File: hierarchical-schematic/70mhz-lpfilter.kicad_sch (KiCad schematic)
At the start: 11 parts, among them J701 In, J702 Out

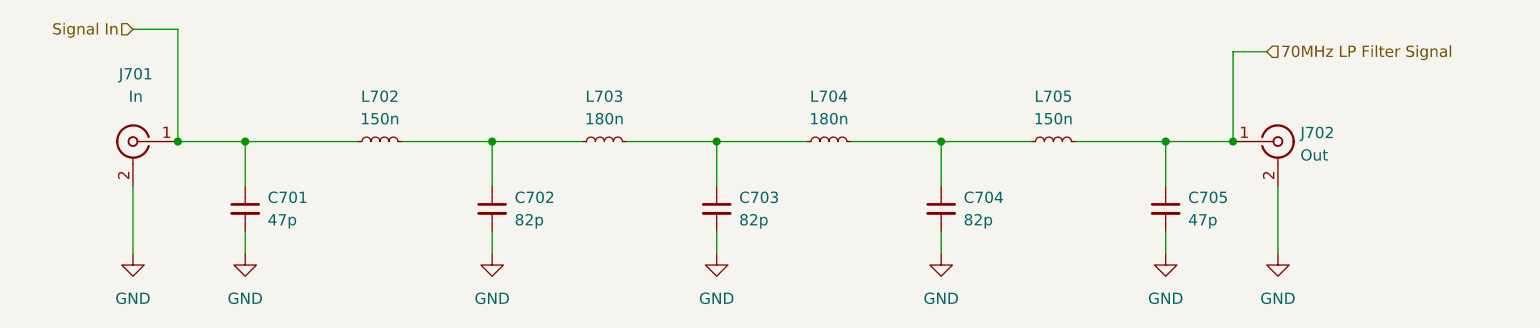
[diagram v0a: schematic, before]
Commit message: updates to hierarchical schematic
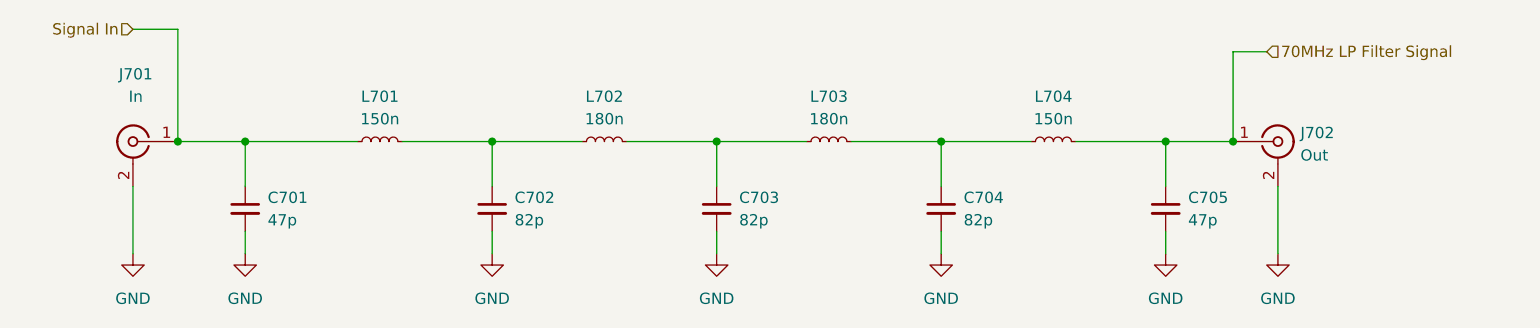
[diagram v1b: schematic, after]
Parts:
- renumbered L702 to L701, L703 to L702, L704 to L703, L705 to L704
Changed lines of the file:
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@@
   (symbol (lib_id "Device:L_Small") (at 212.09 113.03 90) (unit 1)
     (in_bom yes) (on_board yes) (dnp no) (fields_autoplaced)
-    (property "Reference" "L705" (at 212.09 107.95 90)
+    (property "Reference" "L704" (at 212.09 107.95 90)
       (effects (font (size 1.27 1.27)))
     )
@@
       (project "W7ZOI Spectrum Analyzer"
         (path "/d5173421-a214-4849-aa93-f108d8644c8a/7dc681f1-2943-4bbb-a02b-632990122836"
-          (reference "L705") (unit 1)
+          (reference "L704") (unit 1)
         )
       )
@@
   (symbol (lib_id "Device:L_Small") (at 186.69 113.03 90) (unit 1)
     (in_bom yes) (on_board yes) (dnp no) (fields_autoplaced)
-    (property "Reference" "L704" (at 186.69 107.95 90)
+    (property "Reference" "L703" (at 186.69 107.95 90)
       (effects (font (size 1.27 1.27)))
     )
@@
       (project "W7ZOI Spectrum Analyzer"
         (path "/d5173421-a214-4849-aa93-f108d8644c8a/7dc681f1-2943-4bbb-a02b-632990122836"
-          (reference "L704") (unit 1)
+          (reference "L703") (unit 1)
         )
       )
@@
   (symbol (lib_id "Device:L_Small") (at 135.89 113.03 90) (unit 1)
     (in_bom yes) (on_board yes) (dnp no) (fields_autoplaced)
-    (property "Reference" "L702" (at 135.89 107.95 90)
+    (property "Reference" "L701" (at 135.89 107.95 90)
       (effects (font (size 1.27 1.27)))
     )
@@
       (project "W7ZOI Spectrum Analyzer"
         (path "/d5173421-a214-4849-aa93-f108d8644c8a/7dc681f1-2943-4bbb-a02b-632990122836"
-          (reference "L702") (unit 1)
+          (reference "L701") (unit 1)
         )
       )
@@
   (symbol (lib_id "Device:L_Small") (at 161.29 113.03 90) (unit 1)
     (in_bom yes) (on_board yes) (dnp no)
-    (property "Reference" "L703" (at 161.29 107.95 90)
+    (property "Reference" "L702" (at 161.29 107.95 90)
       (effects (font (size 1.27 1.27)))
     )
@@
       (project "W7ZOI Spectrum Analyzer"
         (path "/d5173421-a214-4849-aa93-f108d8644c8a/7dc681f1-2943-4bbb-a02b-632990122836"
-          (reference "L703") (unit 1)
-        )
-      )
+          (reference "L702") (unit 1)
+        )
+      )

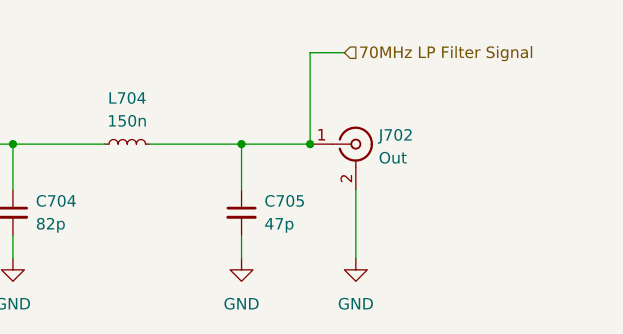
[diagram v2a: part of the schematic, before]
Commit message: updatess to kicad v8
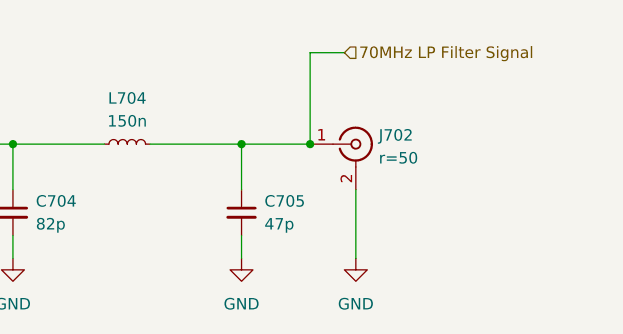
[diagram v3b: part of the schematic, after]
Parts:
- J702: value Out -> ${SIM.PARAMS}
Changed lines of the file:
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@@
 	(title_block
 		(title "Spectrum Analyzer: 70MHz Low Pass Filter")
-		(date "2022-08-23")
+		(date "2022-08-22")
 		(rev "0")
 		(company "Andy McCann KA3KAF and Doug McCann KA3KAG")
@@
 		(shape input)
 		(at 236.22 102.87 0)
-		(fields_autoplaced yes)
 		(effects
 			(font
@@
 		(shape input)
 		(at 107.95 100.33 180)
-		(fields_autoplaced yes)
 		(effects
 			(font
@@
 		(at 199.39 125.73 0)
 		(unit 1)
-		(exclude_from_sim no)
+		(exclude_from_sim yes)
 		(in_bom yes)
 		(on_board yes)
@@
 			)
 		)
-		(property "Description" ""
+		(property "Description" "Power symbol creates a global label with name \"GND\" , ground"
 			(at 199.39 125.73 0)
 			(effects
@@
 		(at 173.99 125.73 0)
 		(unit 1)
-		(exclude_from_sim no)
+		(exclude_from_sim yes)
 		(in_bom yes)
 		(on_board yes)
@@
 			)
 		)
-		(property "Description" ""
+		(property "Description" "Power symbol creates a global label with name \"GND\" , ground"
 			(at 173.99 125.73 0)
 			(effects
@@
 		(at 120.65 125.73 0)
 		(unit 1)
-		(exclude_from_sim no)
+		(exclude_from_sim yes)
 		(in_bom yes)
 		(on_board yes)
@@
 			)
 		)
-		(property "Description" ""
+		(property "Description" "Power symbol creates a global label with name \"GND\" , ground"
 			(at 120.65 125.73 0)
 			(effects
@@
 		(at 173.99 120.65 0)
 		(unit 1)
-		(exclude_from_sim no)
+		(exclude_from_sim yes)
 		(in_bom yes)
 		(on_board yes)
@@
 		(at 148.59 125.73 0)
 		(unit 1)
-		(exclude_from_sim no)
+		(exclude_from_sim yes)
 		(in_bom yes)
 		(on_board yes)
@@
 			)
 		)
-		(property "Description" ""
+		(property "Description" "Power symbol creates a global label with name \"GND\" , ground"
 			(at 148.59 125.73 0)
 			(effects
@@
 		(at 212.09 113.03 90)
 		(unit 1)
-		(exclude_from_sim no)
+		(exclude_from_sim yes)
 		(in_bom yes)
 		(on_board yes)
@@
 		(at 148.59 120.65 0)
 		(unit 1)
-		(exclude_from_sim no)
+		(exclude_from_sim yes)
 		(in_bom yes)
 		(on_board yes)
@@
 		(at 107.95 125.73 0)
 		(unit 1)
-		(exclude_from_sim no)
+		(exclude_from_sim yes)
 		(in_bom yes)
 		(on_board yes)
@@
 			)
 		)
-		(property "Description" ""
+		(property "Description" "Power symbol creates a global label with name \"GND\" , ground"
 			(at 107.95 125.73 0)
 			(effects
@@
 			)
 		)
-		(property "Datasheet" " ~"
+		(property "Datasheet" "~"
 			(at 107.95 113.03 0)
 			(effects
@@
 			)
 		)
-		(property "Description" ""
+		(property "Description" "coaxial connector (BNC, SMA, SMB, SMC, Cinch/RCA, LEMO, ...)"
 			(at 107.95 113.03 0)
 			(effects
@@
 		(at 237.49 125.73 0)
 		(unit 1)
-		(exclude_from_sim no)
+		(exclude_from_sim yes)
 		(in_bom yes)
 		(on_board yes)
@@
 			)
 		)
-		(property "Description" ""
+		(property "Description" "Power symbol creates a global label with name \"GND\" , ground"
 			(at 237.49 125.73 0)
 			(effects
@@
 			)
 		)
-		(property "Value" "Out"
+		(property "Value" "${SIM.PARAMS}"
 			(at 240.03 114.5931 0)
 			(effects
@@
 			)
 		)
-		(property "Datasheet" " ~"
+		(property "Datasheet" "~"
 			(at 237.49 113.03 0)
 			(effects
@@
 			)
 		)
-		(property "Description" ""
+		(property "Description" "coaxial connector (BNC, SMA, SMB, SMC, Cinch/RCA, LEMO, ...)"
+			(at 237.49 113.03 0)
+			(effects
+				(font
+					(size 1.27 1.27)
+				)
+				(hide yes)
+			)
+		)
+		(property "Sim.Device" "R"
+			(at 237.49 113.03 0)
+			(effects
+				(font
+					(size 1.27 1.27)
+				)
+				(hide yes)
+			)
+		)
+		(property "Sim.Pins" "1=+ 2=-"
+			(at 237.49 113.03 0)
+			(effects
+				(font
+					(size 1.27 1.27)
+				)
+				(hide yes)
+			)
+		)
+		(property "Sim.Type" "="
+			(at 237.49 113.03 0)
+			(effects
+				(font
+					(size 1.27 1.27)
+				)
+				(hide yes)
+			)
+		)
+		(property "Sim.Params" "r=50"
 			(at 237.49 113.03 0)
 			(effects
@@
 		(at 199.39 120.65 0)
 		(unit 1)
-		(exclude_from_sim no)
+		(exclude_from_sim yes)
 		(in_bom yes)
 		(on_board yes)
@@
 		(at 224.79 120.65 0)
 		(unit 1)
-		(exclude_from_sim no)
+		(exclude_from_sim yes)
 		(in_bom yes)
 		(on_board yes)
@@
 		(at 186.69 113.03 90)
 		(unit 1)
-		(exclude_from_sim no)
+		(exclude_from_sim yes)
 		(in_bom yes)
 		(on_board yes)
@@
 		(at 135.89 113.03 90)
 		(unit 1)
-		(exclude_from_sim no)
+		(exclude_from_sim yes)
 		(in_bom yes)
 		(on_board yes)
@@
 		(at 224.79 125.73 0)
 		(unit 1)
-		(exclude_from_sim no)
+		(exclude_from_sim yes)
 		(in_bom yes)
 		(on_board yes)
@@
 			)
 		)
-		(property "Description" ""
+		(property "Description" "Power symbol creates a global label with name \"GND\" , ground"
 			(at 224.79 125.73 0)
 			(effects
@@
 		(at 161.29 113.03 90)
 		(unit 1)
-		(exclude_from_sim no)
+		(exclude_from_sim yes)
 		(in_bom yes)
 		(on_board yes)
@@
 		(at 120.65 120.65 0)
 		(unit 1)
-		(exclude_from_sim no)
-		(in_bom yes)
-		(on_board yes)
+		(exclude_from_sim yes)
+		(in_bom yes)
+		(on_board yes)
